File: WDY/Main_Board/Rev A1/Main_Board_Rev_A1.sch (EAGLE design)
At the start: 192 parts, among them J1 22-05-7028-02, J10 22-05-7038-03, J11 22-05-7028-02, J12 22-05-7028-02, J13 22-05-7028-02, J14 22-05-7028-02, J15 22-05-7058-05, J16 22-27-2061-06, J2 22-05-7028-02, J3 22-05-7048-04, J4 22-05-7048-04, J5 1241050-5, J6 90814-0208, J7 90814-0206, J8 90814-0208, J9 22-05-7038-03, K1 G6K-2G-Y, K2 G6K-2G-Y, K3 G6K-2G-Y, K4 G6K-2G-Y, P1 RB1-125BAG1A, SW1 B3FS-1015, SW2 B3FS-1015, T1 MMBT2222AL, U1 LPC1768FBD100, U11 SN74LVC3G17DCTR, U2 SN74LVC3G17DCTR, U3 SN74LVC3G17DCTR, U4 TPL0401A, U5 AT24C512C-SSHM-B, U6 SN74LVC2G17DBVR, U7 SN74LVC2G17DBVR, U8 LT1767EMS8E-5PBF, U9 TC1264-3.3, X1 FC-135, X2 MSTBA2

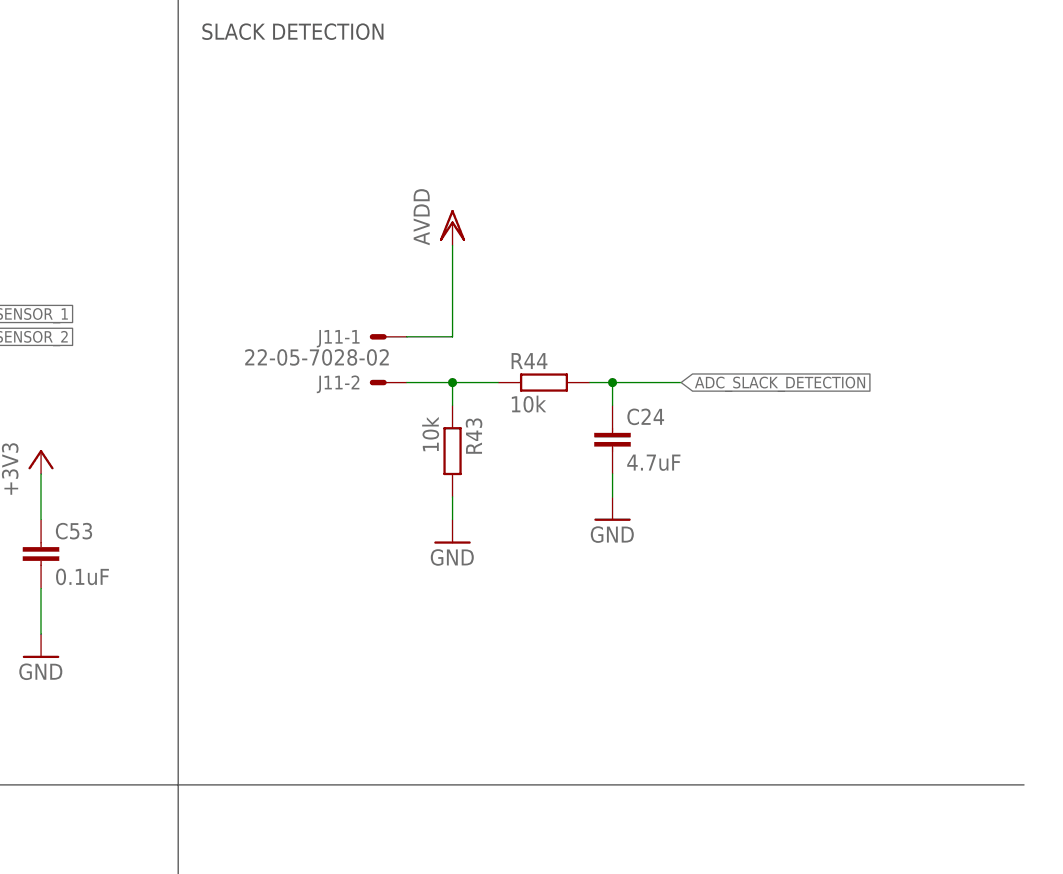
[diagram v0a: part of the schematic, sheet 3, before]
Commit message: Rename board to Main_Board_Rev_A1
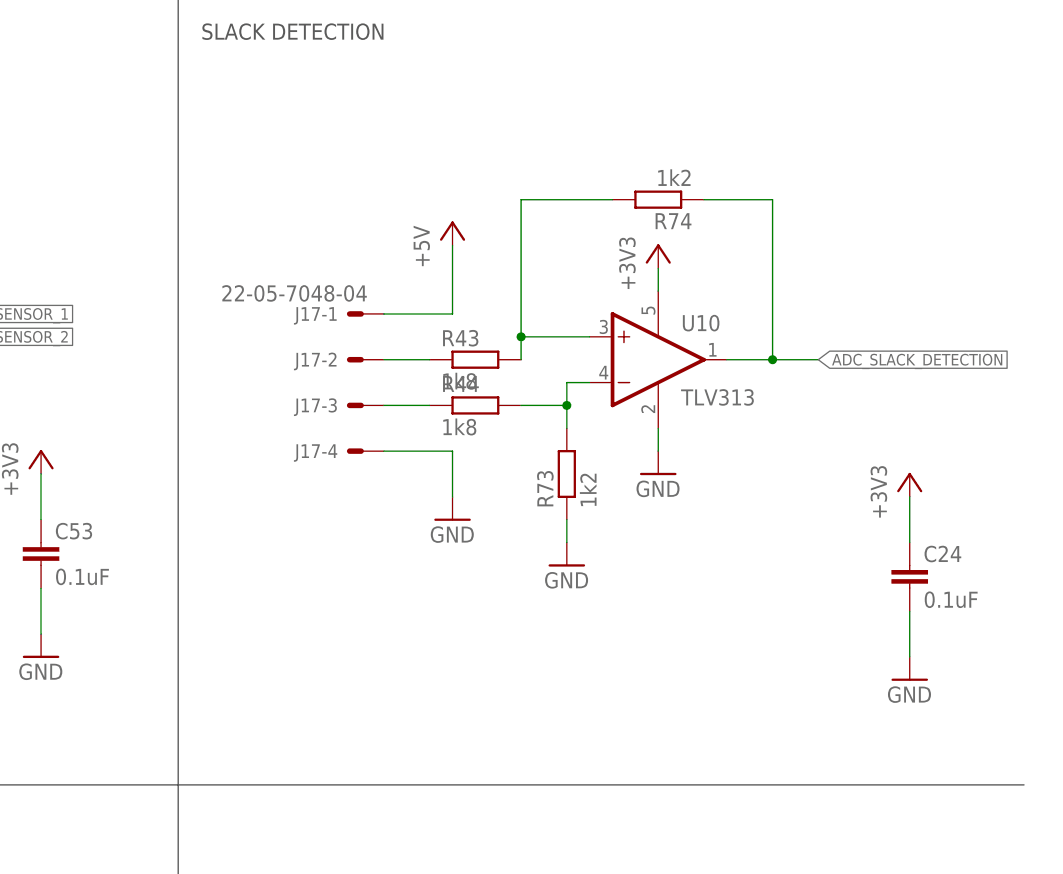
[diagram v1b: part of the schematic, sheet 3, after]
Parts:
- removed J11: 22-05-7028-02, con-molex:22-05-7028-02
- added J17: 22-05-7048-04, con-molex:22-05-7048-04
- added R73, R74: 1k2, rcl:R-EU_R0603
- added U10: TLV313, ti:TLV313
- C24: value 4.7uF -> 0.1uF
- R43, R44: value 10k -> 1k8
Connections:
- new net N$31: J17-2.S, R43.1
- new net N$61: R43.2, R74.2, U10.+IN
- new net N$68: J17-3.S, R44.1
- net +3V3: now also C24.1, U10.V+
- net +5V: now also J17-1.S
- net ADC_SLACK_DETECTION: now also R74.1, U10.OUT; no longer C24.1, R44.2
- net AVDD: no longer J11-1.S
- net GND: now also J17-4.S, R73.1, U10.V-; no longer R43.2
- net N$67: now also R44.2, R73.2, U10.-IN; no longer J11-2.S, R43.1, R44.1
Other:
- moved on the sheet: C24, R43, R44

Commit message: Update libraries
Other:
- moved on the sheet: J16-1, J16-2, J16-3, J16-4, J16-5, J16-6

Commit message: Add Cortex M debug connector
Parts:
- added J11: FTSH-105-01-L-DV, con-samtec:FTSH-105-01-L-DV
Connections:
- removed net JTAG_RST: J5.P$5
- net +3V3: now also J11-1.S
- net GND: now also J11-3.S, J11-5.S, J11-9.S
- net JTAG_TCK: now also J11-4.S
- net JTAG_TDI: now also J11-8.S
- net JTAG_TDO: now also J11-6.S
- net JTAG_TMS: now also J11-2.S
- net RESET: now also J11-10.S, J5.P$5
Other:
- moved on the sheet: J16-1, J16-2, J16-3, J16-4, J16-5, J16-6, J5, LED1, R22, R23, R24, R25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

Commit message: Add name and fiducial
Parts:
- added JP2, JP3, JP4, JP5: FIDUCIAL1.5X3, SparkFun:FIDUCIAL1.5X3
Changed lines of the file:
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@@
 <part name="+3V48" library="supply1" deviceset="+3V3" device=""/>
 <part name="GND91" library="supply1" deviceset="GND" device=""/>
+<part name="JP2" library="SparkFun" deviceset="FIDUCIAL" device="1.5X3"/>
+<part name="JP3" library="SparkFun" deviceset="FIDUCIAL" device="1.5X3"/>
+<part name="JP4" library="SparkFun" deviceset="FIDUCIAL" device="1.5X3"/>
+<part name="JP5" library="SparkFun" deviceset="FIDUCIAL" device="1.5X3"/>
 </parts>
 <sheets>
@@
 <instance part="+3V30" gate="G$1" x="139.7" y="193.04"/>
 <instance part="+3V44" gate="G$1" x="360.68" y="144.78"/>
+<instance part="JP2" gate="G$1" x="344.678" y="21.59"/>
+<instance part="JP3" gate="G$1" x="348.488" y="21.59"/>
+<instance part="JP4" gate="G$1" x="352.298" y="21.59"/>
+<instance part="JP5" gate="G$1" x="356.362" y="21.59"/>
 </instances>
 <busses>

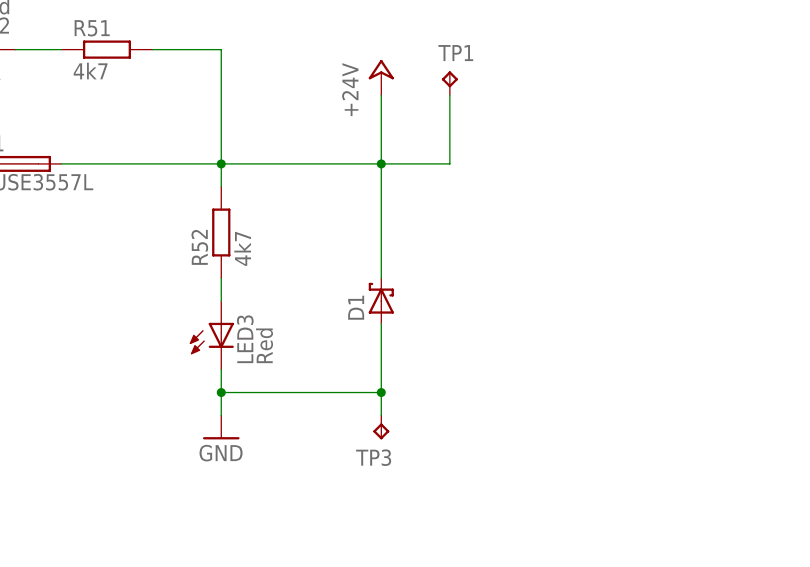
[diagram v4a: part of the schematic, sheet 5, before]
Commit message: Add LED value
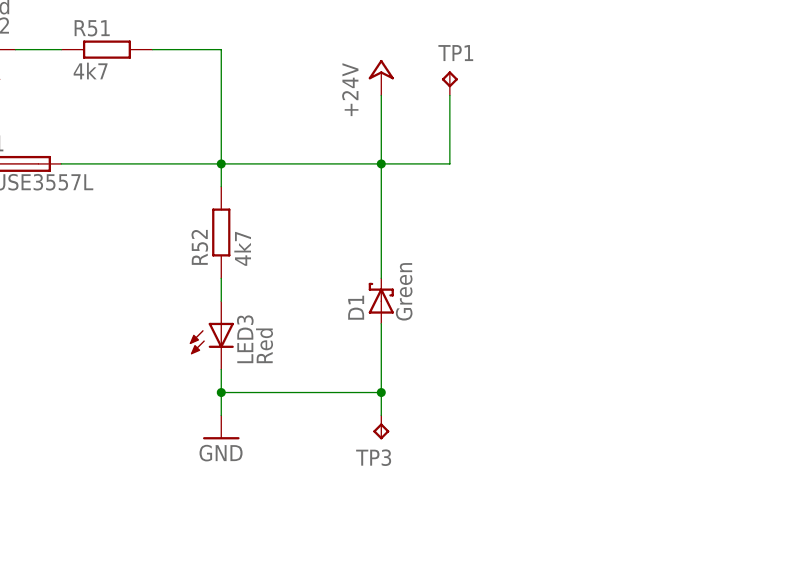
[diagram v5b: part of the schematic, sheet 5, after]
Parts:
- D1: value (none) -> Green
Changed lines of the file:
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@@
 <part name="LED3" library="led" deviceset="LED" device="CHIPLED_0603" value="Red"/>
 <part name="GND63" library="supply1" deviceset="GND" device=""/>
-<part name="D1" library="diode" deviceset="STPS3L40?" device="UF"/>
+<part name="D1" library="diode" deviceset="STPS3L40?" device="UF" value="Green"/>
 <part name="GND64" library="supply1" deviceset="GND" device=""/>
 <part name="TP1" library="testpad" deviceset="TP" device="B1,27"/>
@@
 <instance part="+3V8" gate="G$1" x="327.66" y="71.12"/>
 <instance part="GND16" gate="1" x="327.66" y="38.1"/>
-<instance part="U$4" gate="G$1" x="304.8" y="58.42" rot="MR0"/>
+<instance part="U$4" gate="G" x="304.8" y="58.42" rot="MR0"/>
 <instance part="GND17" gate="1" x="360.68" y="45.72"/>
 <instance part="+3V9" gate="G$1" x="360.68" y="71.12"/>
@@
 <pinref part="GND16" gate="1" pin="GND"/>
 <wire x1="327.66" y1="45.72" x2="327.66" y2="40.64" width="0.1524" layer="91"/>
-<pinref part="U$4" gate="G$1" pin="VSS"/>
+<pinref part="U$4" gate="G" pin="VSS"/>
 <wire x1="327.66" y1="45.72" x2="322.58" y2="45.72" width="0.1524" layer="91"/>
-<pinref part="U$4" gate="G$1" pin="STBY"/>
+<pinref part="U$4" gate="G" pin="STBY"/>
 <wire x1="327.66" y1="50.8" x2="322.58" y2="50.8" width="0.1524" layer="91"/>
 <wire x1="327.66" y1="45.72" x2="327.66" y2="50.8" width="0.1524" layer="91"/>
@@
 </segment>
 <segment>
-<pinref part="U$4" gate="G$1" pin="VDD"/>
+<pinref part="U$4" gate="G" pin="VDD"/>
 <pinref part="+3V8" gate="G$1" pin="+3V3"/>
 <wire x1="322.58" y1="63.5" x2="327.66" y2="63.5" width="0.1524" layer="91"/>
@@
 <net name="CAN_RX" class="1">
 <segment>
-<pinref part="U$4" gate="G$1" pin="RXD"/>
+<pinref part="U$4" gate="G" pin="RXD"/>
 <wire x1="322.58" y1="55.88" x2="330.2" y2="55.88" width="0.1524" layer="91"/>
 <label x="330.2" y="55.88" size="1.27" layer="95" xref="yes"/>
@@
 <net name="CAN_TX" class="1">
 <segment>
-<pinref part="U$4" gate="G$1" pin="TXD"/>
+<pinref part="U$4" gate="G" pin="TXD"/>
 <wire x1="322.58" y1="58.42" x2="330.2" y2="58.42" width="0.1524" layer="91"/>
 <label x="330.2" y="58.42" size="1.27" layer="95" xref="yes"/>
@@
 <net name="CAN_L" class="1">
 <segment>
-<pinref part="U$4" gate="G$1" pin="CANL"/>
+<pinref part="U$4" gate="G" pin="CANL"/>
 <wire x1="287.02" y1="53.34" x2="279.4" y2="53.34" width="0.1524" layer="91"/>
 <label x="279.4" y="53.34" size="1.27" layer="95" rot="R180" xref="yes"/>
@@
 <net name="CAN_H" class="1">
 <segment>
-<pinref part="U$4" gate="G$1" pin="CANH"/>
+<pinref part="U$4" gate="G" pin="CANH"/>
 <wire x1="287.02" y1="50.8" x2="279.4" y2="50.8" width="0.1524" layer="91"/>
 <label x="279.4" y="50.8" size="1.27" layer="95" rot="R180" xref="yes"/>
@@
 <net name="CAN_SPLIT" class="1">
 <segment>
-<pinref part="U$4" gate="G$1" pin="SPLIT"/>
+<pinref part="U$4" gate="G" pin="SPLIT"/>
 <wire x1="287.02" y1="60.96" x2="279.4" y2="60.96" width="0.1524" layer="91"/>
 <label x="279.4" y="60.96" size="1.27" layer="95" rot="R180" xref="yes"/>

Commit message: Update Main_Board_Rev_A1 schematics and board and con-molex lib
* Add solder jumper to +5V supplied by UART
* Swap TXDO and RXDO UART signals
* Simplify 22-27-2061-06 package in con-molex.lbr
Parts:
- added SJ3: SOLDERJUMPERNO, SparkFun-Passives:SOLDERJUMPERNO
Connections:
- new net N$69: J16-2.S, SJ3.1
- net +5V: now also SJ3.2; no longer J16-2.S
- net ISP_RXDO: now also J16-4.S; no longer J16-5.S
- net ISP_TXDO: now also J16-5.S; no longer J16-4.S
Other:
- note added: "UART"
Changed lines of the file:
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@@
 <part name="R70" library="rcl" deviceset="R-EU_" device="R0603" value="100"/>
 <part name="J16" library="con-molex" deviceset="22-?-06" device="27-2061"/>
-<part name="P+23" library="supply1" deviceset="+5V" device=""/>
 <part name="GND90" library="supply1" deviceset="GND" device=""/>
 <part name="TP3" library="testpad" deviceset="TP" device="B1,27"/>
-<part name="JP1" library="exmachina" deviceset="BC-2-?" device="P"/>
+<part name="JP1" library="exmachina" deviceset="BC-2?" device="-P"/>
 <part name="R71" library="rcl" deviceset="R-EU_" device="R0603" value="0R"/>
 <part name="R72" library="rcl" deviceset="R-EU_" device="R0603" value="0R"/>
@@
 <part name="JP4" library="SparkFun" deviceset="FIDUCIAL" device="1.5X3"/>
 <part name="JP5" library="SparkFun" deviceset="FIDUCIAL" device="1.5X3"/>
+<part name="SJ3" library="SparkFun-Passives" deviceset="SOLDERJUMPER" device="NO"/>
+<part name="P+23" library="supply1" deviceset="+5V" device=""/>
 </parts>
 <sheets>
@@
 <instance part="+3V8" gate="G$1" x="327.66" y="71.12"/>
 <instance part="GND16" gate="1" x="327.66" y="38.1"/>
-<instance part="U$4" gate="G" x="304.8" y="58.42" rot="MR0"/>
+<instance part="U$4" gate="G$1" x="304.8" y="58.42" rot="MR0"/>
 <instance part="GND17" gate="1" x="360.68" y="45.72"/>
 <instance part="+3V9" gate="G$1" x="360.68" y="71.12"/>
@@
 <pinref part="GND16" gate="1" pin="GND"/>
 <wire x1="327.66" y1="45.72" x2="327.66" y2="40.64" width="0.1524" layer="91"/>
-<pinref part="U$4" gate="G" pin="VSS"/>
+<pinref part="U$4" gate="G$1" pin="VSS"/>
 <wire x1="327.66" y1="45.72" x2="322.58" y2="45.72" width="0.1524" layer="91"/>
-<pinref part="U$4" gate="G" pin="STBY"/>
+<pinref part="U$4" gate="G$1" pin="STBY"/>
 <wire x1="327.66" y1="50.8" x2="322.58" y2="50.8" width="0.1524" layer="91"/>
 <wire x1="327.66" y1="45.72" x2="327.66" y2="50.8" width="0.1524" layer="91"/>
@@
 </segment>
 <segment>
-<pinref part="U$4" gate="G" pin="VDD"/>
+<pinref part="U$4" gate="G$1" pin="VDD"/>
 <pinref part="+3V8" gate="G$1" pin="+3V3"/>
 <wire x1="322.58" y1="63.5" x2="327.66" y2="63.5" width="0.1524" layer="91"/>
@@
 <net name="CAN_RX" class="1">
 <segment>
-<pinref part="U$4" gate="G" pin="RXD"/>
+<pinref part="U$4" gate="G$1" pin="RXD"/>
 <wire x1="322.58" y1="55.88" x2="330.2" y2="55.88" width="0.1524" layer="91"/>
 <label x="330.2" y="55.88" size="1.27" layer="95" xref="yes"/>
@@
 <net name="CAN_TX" class="1">
 <segment>
-<pinref part="U$4" gate="G" pin="TXD"/>
+<pinref part="U$4" gate="G$1" pin="TXD"/>
 <wire x1="322.58" y1="58.42" x2="330.2" y2="58.42" width="0.1524" layer="91"/>
 <label x="330.2" y="58.42" size="1.27" layer="95" xref="yes"/>
@@
 <net name="CAN_L" class="1">
 <segment>
-<pinref part="U$4" gate="G" pin="CANL"/>
+<pinref part="U$4" gate="G$1" pin="CANL"/>
 <wire x1="287.02" y1="53.34" x2="279.4" y2="53.34" width="0.1524" layer="91"/>
 <label x="279.4" y="53.34" size="1.27" layer="95" rot="R180" xref="yes"/>
@@
 <net name="CAN_H" class="1">
 <segment>
-<pinref part="U$4" gate="G" pin="CANH"/>
+<pinref part="U$4" gate="G$1" pin="CANH"/>
 <wire x1="287.02" y1="50.8" x2="279.4" y2="50.8" width="0.1524" layer="91"/>
 <label x="279.4" y="50.8" size="1.27" layer="95" rot="R180" xref="yes"/>
@@
 <net name="CAN_SPLIT" class="1">
 <segment>
-<pinref part="U$4" gate="G" pin="SPLIT"/>
+<pinref part="U$4" gate="G$1" pin="SPLIT"/>
 <wire x1="287.02" y1="60.96" x2="279.4" y2="60.96" width="0.1524" layer="91"/>
 <label x="279.4" y="60.96" size="1.27" layer="95" rot="R180" xref="yes"/>
@@
 <wire x1="289.56" y1="105.156" x2="289.56" y2="24.13" width="0.1524" layer="97"/>
 <wire x1="121.92" y1="105.156" x2="121.92" y2="3.81" width="0.1524" layer="97"/>
+<text x="101.6" y="251.46" size="1.778" layer="97">UART</text>
 </plain>
 <instances>
@@
 <instance part="J16" gate="-5" x="121.92" y="220.98" rot="MR0"/>
 <instance part="J16" gate="-6" x="121.92" y="215.9" rot="MR0"/>
-<instance part="P+23" gate="1" x="137.16" y="248.92"/>
 <instance part="GND90" gate="1" x="132.08" y="208.28"/>
 <instance part="J17" gate="-1" x="309.88" y="157.48" rot="MR0"/>
@@
 <instance part="+3V48" gate="G$1" x="294.64" y="248.92"/>
 <instance part="GND91" gate="1" x="294.64" y="205.74"/>
+<instance part="SJ3" gate="1" x="142.24" y="236.22"/>
+<instance part="P+23" gate="1" x="149.86" y="241.3"/>
 </instances>
 <busses>
@@
 </segment>
 <segment>
-<pinref part="J16" gate="-2" pin="S"/>
-<wire x1="124.46" y1="236.22" x2="137.16" y2="236.22" width="0.1524" layer="91"/>
-<wire x1="137.16" y1="236.22" x2="137.16" y2="246.38" width="0.1524" layer="91"/>
-<pinref part="P+23" gate="1" pin="+5V"/>
-</segment>
-<segment>
 <wire x1="312.42" y1="157.48" x2="320.04" y2="157.48" width="0.1524" layer="91"/>
 <wire x1="320.04" y1="157.48" x2="320.04" y2="165.1" width="0.1524" layer="91"/>
 <pinref part="J17" gate="-1" pin="S"/>
 <pinref part="P+24" gate="1" pin="+5V"/>
+</segment>
+<segment>
+<pinref part="P+23" gate="1" pin="+5V"/>
+<pinref part="SJ3" gate="1" pin="2"/>
+<wire x1="149.86" y1="238.76" x2="149.86" y2="236.22" width="0.1524" layer="91"/>
+<wire x1="149.86" y1="236.22" x2="147.32" y2="236.22" width="0.1524" layer="91"/>
 </segment>
 </net>
@@
 </segment>
 </net>
-<net name="ISP_TXDO" class="1">
+<net name="ISP_RXDO" class="1">
 <segment>
 <pinref part="J16" gate="-4" pin="S"/>
 <wire x1="124.46" y1="226.06" x2="144.78" y2="226.06" width="0.1524" layer="91"/>
 <label x="144.78" y="226.06" size="1.27" layer="95" xref="yes"/>
-</segment>
-</net>
-<net name="ISP_RXDO" class="1">
-<segment>
-<pinref part="J16" gate="-5" pin="S"/>
-<wire x1="124.46" y1="220.98" x2="144.78" y2="220.98" width="0.1524" layer="91"/>
-<label x="144.78" y="220.98" size="1.27" layer="95" xref="yes"/>
 </segment>
 </net>
@@
 </segment>
 </net>
+<net name="ISP_TXDO" class="1">
+<segment>
+<pinref part="J16" gate="-5" pin="S"/>
+<wire x1="124.46" y1="220.98" x2="144.78" y2="220.98" width="0.1524" layer="91"/>
+<label x="144.78" y="220.98" size="1.27" layer="95" xref="yes"/>
+</segment>
+</net>
+<net name="N$69" class="0">
+<segment>
+<pinref part="SJ3" gate="1" pin="1"/>
+<pinref part="J16" gate="-2" pin="S"/>
+<wire x1="137.16" y1="236.22" x2="124.46" y2="236.22" width="0.1524" layer="91"/>
+</segment>
+</net>
